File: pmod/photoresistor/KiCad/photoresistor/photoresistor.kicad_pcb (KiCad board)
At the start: 2 copper layers, 17 x 17 mm, 3 parts, among them J2 Conn_01x06_Pin

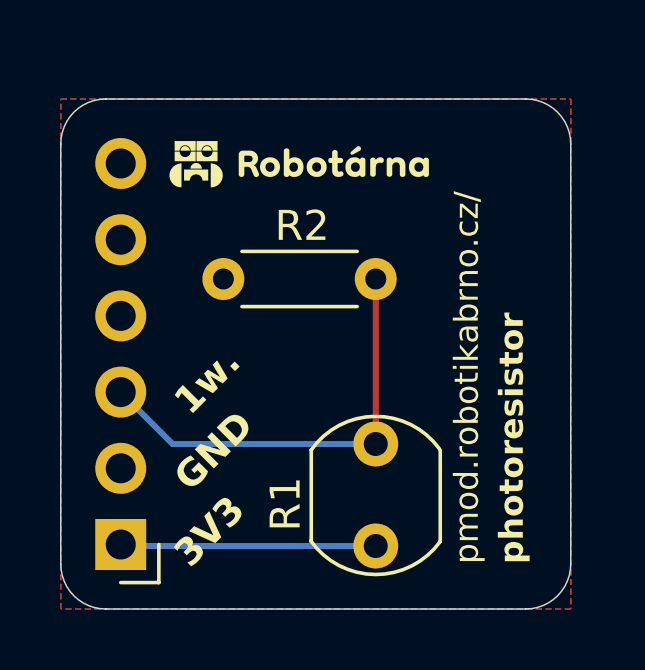
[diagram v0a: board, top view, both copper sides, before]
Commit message: minor fixes and mounting hole added
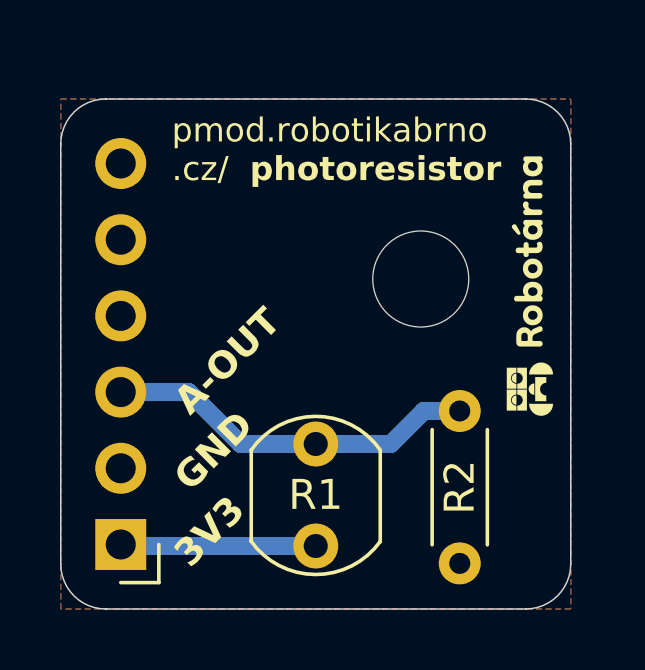
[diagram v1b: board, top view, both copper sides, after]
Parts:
- added H1: MountingHole, MountingHole:MountingHole_3.2mm_M3_DIN965, F.Cu at (133.5, 99.0)
- moved R2 5.22 mm to (134.8, 103.4), turned to -90 degrees
- moved R1 2.00 mm to (130.0, 107.9)
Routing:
- net GPIO: track 14.7 -> 12.5 mm
- net +3V3: track 8.59 -> 6.59 mm
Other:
- board text added: "A-OUT"
- board text added: "pmod.robotikabrno .cz/"
- board text removed: "1w."
- board text removed: "pmod.robotikabrno.cz/"
